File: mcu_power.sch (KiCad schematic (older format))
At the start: 26 parts

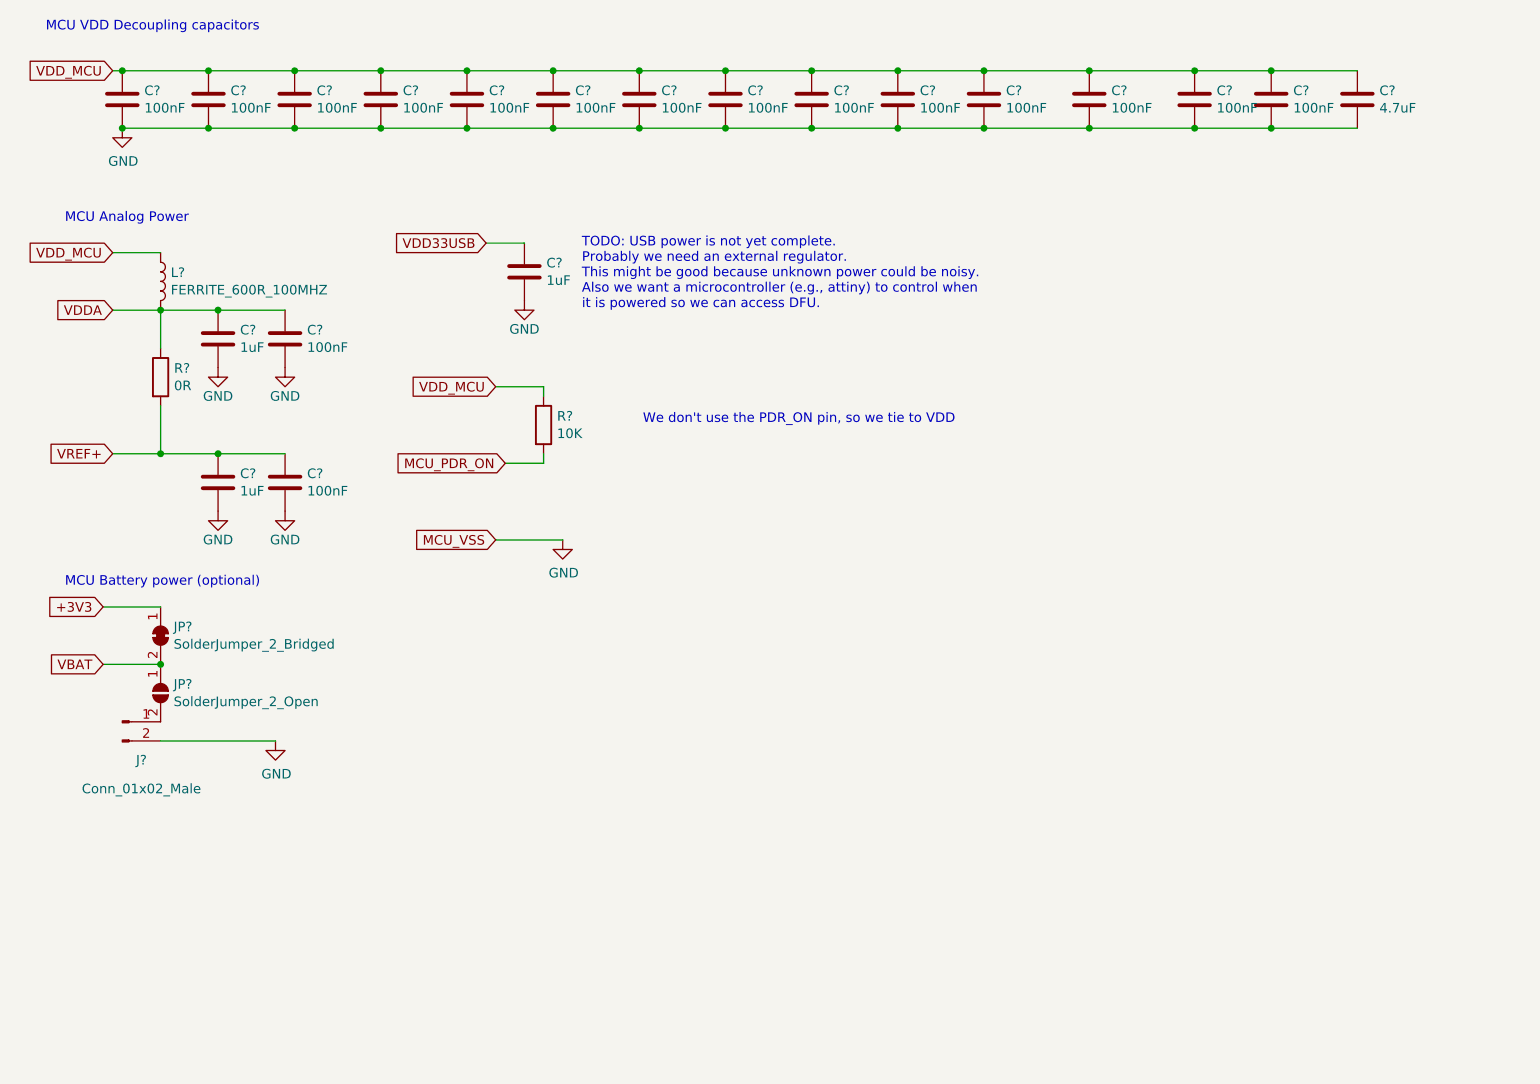
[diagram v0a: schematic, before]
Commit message: First proposed pin layout of SODIMM connector
Will need to add GPIO / ADC pins as needed, but let's wait to see if we don't
need to use more pins.

Double-checked and fixed CODEC and MCU's power supply.
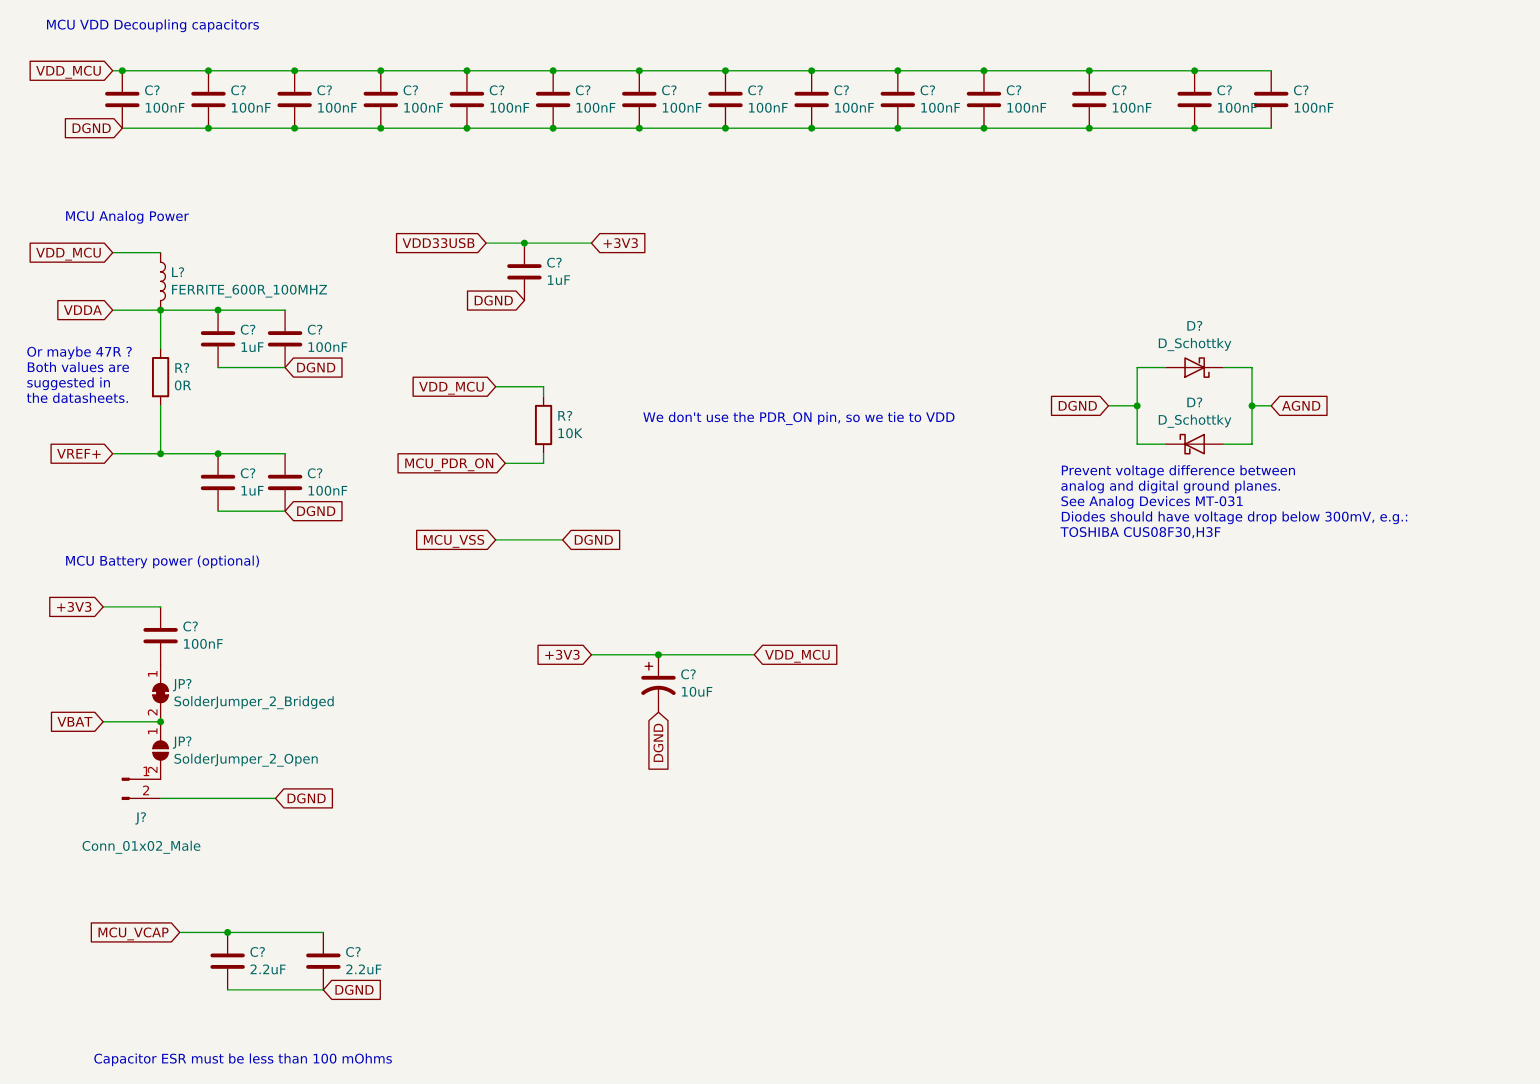
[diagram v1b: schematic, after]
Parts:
- removed C?: 4.7uF, symbol Device:C
- added C?: 10uF, symbol Device:CP1
- added C?: 100nF, symbol Device:C
- added C? (x2): 2.2uF, symbol Device:C
- added D? (x2): D_Schottky, symbol Device:D_Schottky
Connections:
- net VDD33USB is gone; now on net +3V3: C?.1
- net VDD_MCU is gone; now on net +3V3: C?.1, C?.1, C?.1, C?.1, C?.1, C?.1, C?.1, C?.1, C?.1, C?.1, C?.1, C?.1, C?.1, C?.1, L?.1, R?.1
- net +3V3: now also C?.1, C?.1; no longer JP?.1 (A)
- net GND renamed DGND
- net DGND: now also C?.2, C?.2, C?.2, D?.1 (K), D?.2 (A)
- new net: C?.2, JP?.1 (A)
- new net AGND: D?.1 (K), D?.2 (A)
- new net MCU_VCAP: C?.1, C?.1
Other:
- note added: "Capacitor ESR must be less than 100 mOhms"
- note added: "Or maybe 47R ?\nBoth values are \nsuggested in \nthe datasheets."
- note added: "Prevent voltage difference between\nanalog and digital ground planes.\nSee Analog Devices MT-031\nDiodes should have voltage drop below 300mV, e.g.:\nTOSHIBA CUS08F30,H3F"
- note removed: "TODO: USB power is not yet complete.\nProbably we need an external regulator. \nThis might be good because unknown power could be noisy. \nAlso we want a microcontroller (e.g., attiny) to control when \nit is powered so we can access DFU."
- moved on the sheet: J?, JP?
